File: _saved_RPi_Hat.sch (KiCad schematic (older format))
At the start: 28 parts, among them J3 RPi_GPIO, P1 3Sip100, P2 4Sip200, P3 2Sip200, P4 SMA, P5 CONN_01X02, Q1 BC237, U1 LM7805

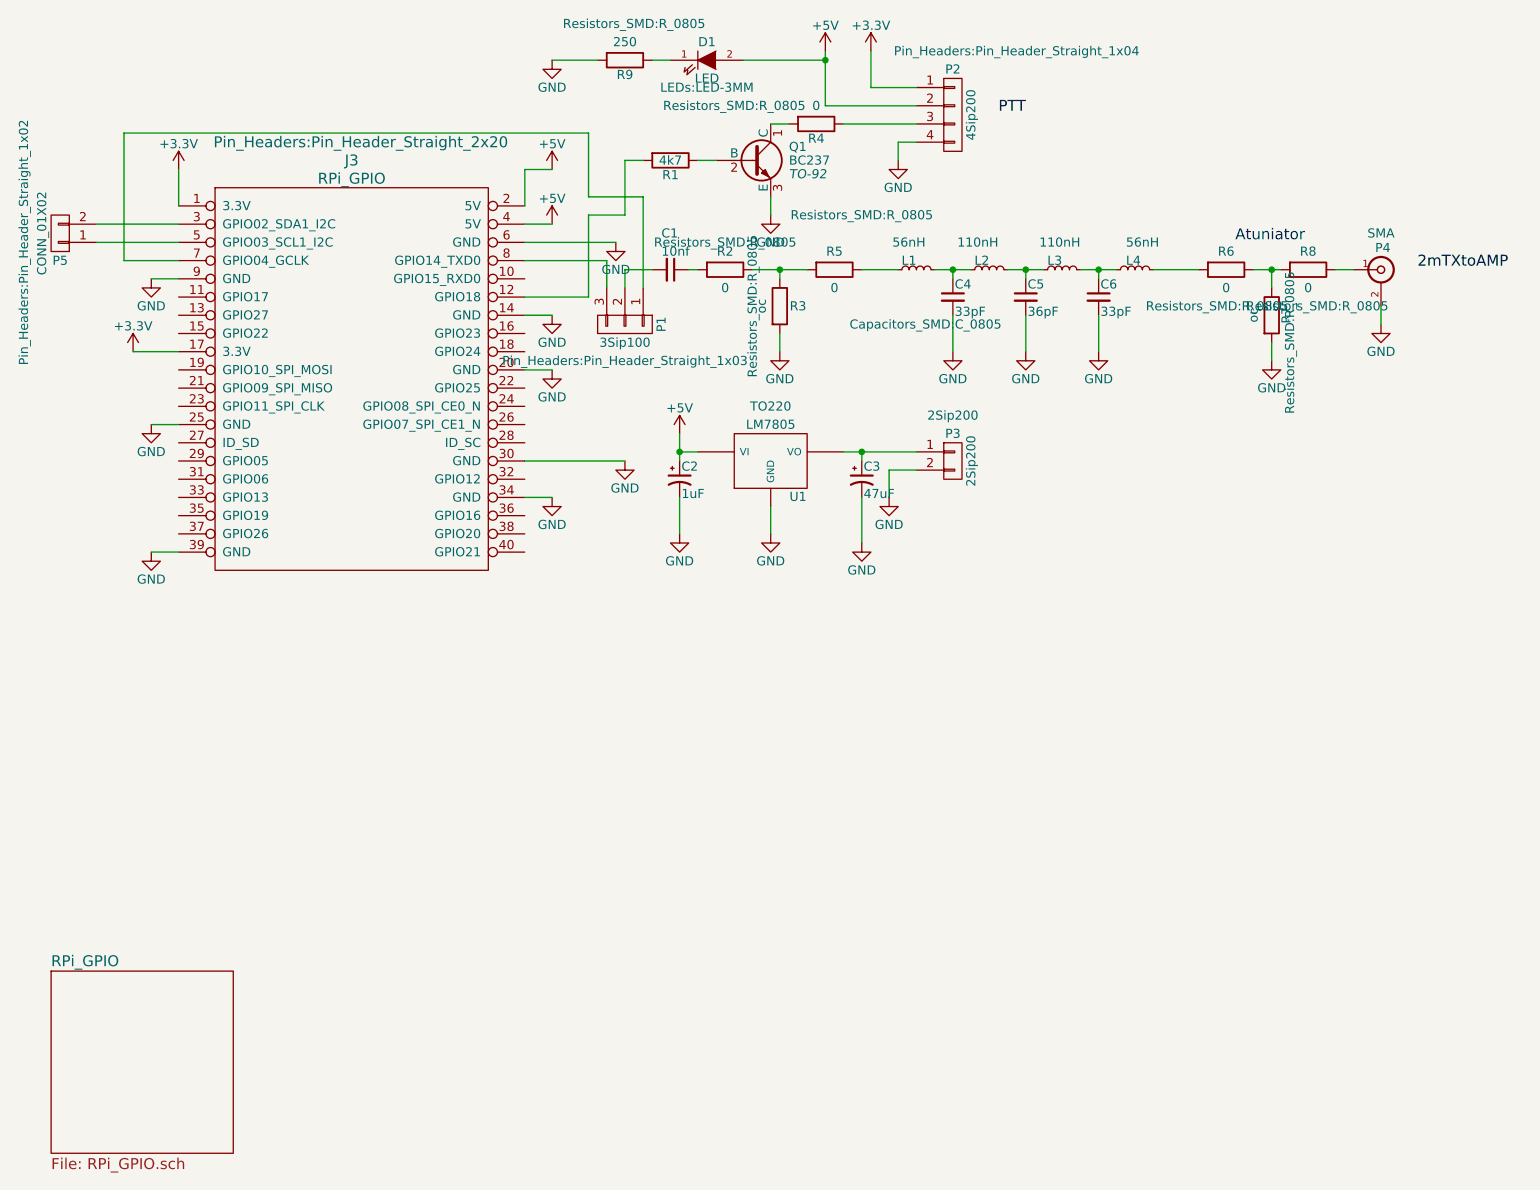
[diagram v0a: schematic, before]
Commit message: added annotation and module details
sma connector footprint still not corect
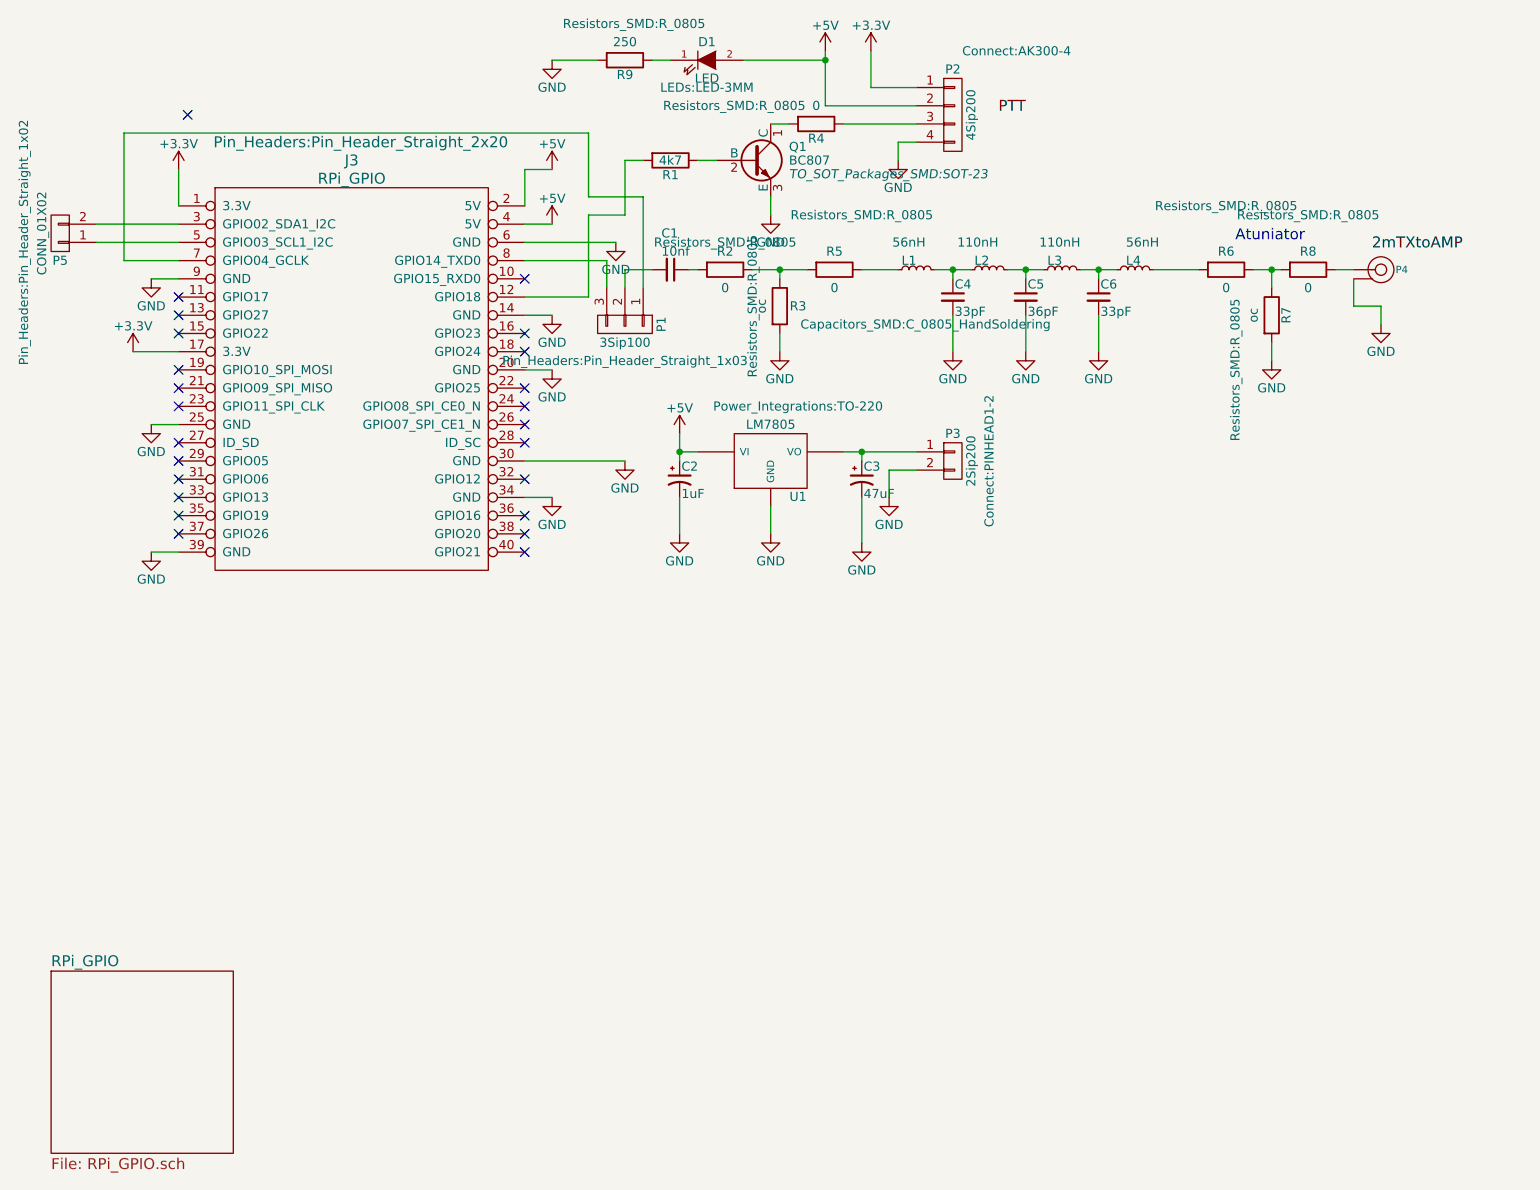
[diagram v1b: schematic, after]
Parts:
- removed P4: SMA, symbol BNC
- added P4: SMA, symbol SMA
- C2: footprint (none) -> Capacitors_SMD:c_elec_4x5.7
- C3: footprint (none) -> Capacitors_SMD:c_elec_6.3x5.7
- C4: footprint Capacitors_SMD:C_0805 -> Capacitors_SMD:C_0805_HandSoldering
- P2: footprint Pin_Headers:Pin_Header_Straight_1x04 -> Connect:AK300-4
- P3: footprint 2Sip200 -> Connect:PINHEAD1-2
- Q1: value BC237 -> BC807; footprint TO-92 -> TO_SOT_Packages_SMD:SOT-23
- U1: footprint TO220 -> Power_Integrations:TO-220
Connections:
- net GND: now also P4.2
- net at R8.1: now also P4.1
- no-connect marks 0 -> 24
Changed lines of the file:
@@
 LIBS:valves
 LIBS:RPi_Hat-cache
+LIBS:SMA
 EELAYER 25 0
 EELAYER END
@@
 F 0 "C4" H 5860 2270 50  0000 L CNN
 F 1 "33pF" H 5860 2120 50  0000 L CNN
-F 2 "Capacitors_SMD:C_0805" H 5700 2050 50  0000 C CNN
+F 2 "Capacitors_SMD:C_0805_HandSoldering" H 5700 2050 50  0000 C CNN
 F 3 "" H 5850 2200 50  0000 C CNN
 	1    5850 2200
@@
 F 0 "R6" V 7250 2050 50  0000 C CNN
 F 1 "0" V 7450 2050 50  0000 C CNN
-F 2 "Resistors_SMD:R_0805" V 7550 2000 50  0000 C CNN
+F 2 "Resistors_SMD:R_0805" V 7000 2050 50  0000 C CNN
 F 3 "" H 7350 2050 50  0000 C CNN
 	1    7350 2050
@@
 F 0 "R8" V 7700 2050 50  0000 C CNN
 F 1 "0" V 7900 2050 50  0000 C CNN
-F 2 "Resistors_SMD:R_0805" V 8000 2100 50  0000 C CNN
+F 2 "Resistors_SMD:R_0805" V 7500 2050 50  0000 C CNN
 F 3 "" H 7800 2050 50  0000 C CNN
 	1    7800 2050
@@
 F 0 "R7" V 7680 2300 50  0000 C CNN
 F 1 "oc" V 7500 2300 50  0000 C CNN
-F 2 "Resistors_SMD:R_0805" V 7700 2150 50  0000 C CNN
+F 2 "Resistors_SMD:R_0805" V 7400 2000 50  0000 C CNN
 F 3 "" H 7600 2300 50  0000 C CNN
 	1    7600 2300
-	1    0    0    -1
-$EndComp
-$Comp
-L BNC P4
-U 1 1 5873BD61
-P 8200 2050
-F 0 "P4" H 8210 2170 50  0000 C CNN
-F 1 "SMA" H 8200 2250 50  0000 C CNN
-F 2 "" H 8200 2050 50  0001 C CNN
-F 3 "" H 8200 2050 50  0000 C CNN
-	1    8200 2050
 	1    0    0    -1
 $EndComp
@@
 P 4750 1450
 F 0 "Q1" H 4950 1525 50  0000 L CNN
-F 1 "BC237" H 4950 1450 50  0000 L CNN
-F 2 "TO-92" H 4950 1375 50  0000 L CIN
+F 1 "BC807" H 4950 1450 50  0000 L CNN
+F 2 "TO_SOT_Packages_SMD:SOT-23" H 4950 1375 50  0000 L CIN
 F 3 "" H 4750 1450 50  0000 L CNN
 	1    4750 1450
@@
 F 0 "P2" H 5850 1450 50  0000 C CNN
 F 1 "4Sip200" V 5950 1200 50  0000 C CNN
-F 2 "Pin_Headers:Pin_Header_Straight_1x04" H 6200 1550 50  0000 C CNN
+F 2 "Connect:AK300-4" H 6200 1550 50  0000 C CNN
 F 3 "" H 5850 1200 50  0000 C CNN
 	1    5850 1200
@@
 Text Label 6100 1200 0    60   ~ 0
 PTT
-Text Label 8400 2050 0    60   ~ 0
+Text Label 8150 1950 0    60   ~ 0
 2mTXtoAMP
 $Comp
@@
 F 0 "P3" H 5850 3250 50  0000 C CNN
 F 1 "2Sip200" V 5950 3100 50  0000 C CNN
-F 2 "2Sip200" H 5850 3350 50  0000 C CNN
+F 2 "Connect:PINHEAD1-2" V 6050 3100 50  0000 C CNN
 F 3 "" H 5850 3100 50  0000 C CNN
 	1    5850 3100
@@
 F 0 "C2" H 4360 3270 50  0000 L CNN
 F 1 "1uF" H 4360 3120 50  0000 L CNN
-F 2 "" H 4350 3200 50  0001 C CNN
+F 2 "Capacitors_SMD:c_elec_4x5.7" H 4350 3200 50  0001 C CNN
 F 3 "" H 4350 3200 50  0000 C CNN
 	1    4350 3200
@@
 F 0 "C3" H 5360 3270 50  0000 L CNN
 F 1 "47uF" H 5360 3120 50  0000 L CNN
-F 2 "" H 5350 3200 50  0001 C CNN
+F 2 "Capacitors_SMD:c_elec_6.3x5.7" H 5350 3200 50  0001 C CNN
 F 3 "" H 5350 3200 50  0000 C CNN
 	1    5350 3200
-	1    0    0    -1
-$EndComp
-$Comp
-L LM7805 U1
-U 1 1 5874847B
-P 4850 3100
-F 0 "U1" H 5000 2904 50  0000 C CNN
-F 1 "LM7805" H 4850 3300 50  0000 C CNN
-F 2 "TO220" H 4850 3400 50  0000 C CNN
-F 3 "" H 4850 3100 50  0000 C CNN
-	1    4850 3100
 	1    0    0    -1
 $EndComp
@@
 Connection ~ 7600 2050
 Wire Wire Line
-	8200 2250 8200 2350
-Wire Wire Line
 	7600 2450 7600 2550
 Wire Wire Line
@@
 Wire Wire Line
 	3650 900  3900 900
+NoConn ~ 1600 2200
+NoConn ~ 1600 2300
+NoConn ~ 1600 2400
+NoConn ~ 1600 2600
+NoConn ~ 1600 2700
+NoConn ~ 1600 2800
+NoConn ~ 1600 3000
+NoConn ~ 1600 3100
+NoConn ~ 1600 3200
+NoConn ~ 1600 3300
+NoConn ~ 1600 3400
+NoConn ~ 1600 3500
+NoConn ~ 3500 3600
+NoConn ~ 3500 3500
+NoConn ~ 3500 3400
+NoConn ~ 3500 3200
+NoConn ~ 3500 3000
+NoConn ~ 3500 2900
+NoConn ~ 3500 2800
+NoConn ~ 3500 2700
+NoConn ~ 3500 2500
+NoConn ~ 3500 2400
+NoConn ~ 3500 2100
+NoConn ~ 1650 1200
+$Comp
+L LM7805 U1
+U 1 1 5874847B
+P 4850 3100
+F 0 "U1" H 5000 2904 50  0000 C CNN
+F 1 "LM7805" H 4850 3300 50  0000 C CNN
+F 2 "Power_Integrations:TO-220" H 5000 3400 50  0000 C CNN
+F 3 "" H 4850 3100 50  0000 C CNN
+	1    4850 3100
+	1    0    0    -1
+$EndComp
+$Comp
+L SMA P4
+U 1 1 587D7F9F
+P 8200 2050
+F 0 "P4" H 8280 2050 40  0000 L CNN
+F 1 "SMA" H 8200 2105 30  0001 C TNN
+F 2 "" H 8200 2050 60  0000 C CNN
+F 3 "" H 8200 2050 60  0000 C CNN
+	1    8200 2050
+	1    0    0    -1
+$EndComp
+Wire Wire Line
+	8200 2350 8200 2250
+Wire Wire Line
+	8200 2250 8050 2250
+Wire Wire Line
+	8050 2250 8050 2100
 $EndSCHEMATC
